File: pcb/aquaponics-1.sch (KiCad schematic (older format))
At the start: 20 parts, among them J1 5V Power Source, J2 Screw_Terminal_01x02, J3 Water Level Sensor, J4 Rain Sensor, J5 Conn_01x02_Female, M1 Growbed Pump, M2 Overflow Pump, M3 Fish Feeder, Q1 TIP120, Q2 TIP120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

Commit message: Version 2 board
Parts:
- added J6: Conn_01x04_Female, Connector_PinHeader_2.54mm:PinHeader_1x04_P2.54mm_Vertical, symbol Connector:Conn_01x04_Female
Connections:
- net +5V: now also J6.3 (Pin_3)
- net GND1: now also J6.4 (Pin_4)
- net at U1.23 (A4/D18): now also J6.1 (Pin_1)
- net at U1.24 (A5/D19): now also J6.2 (Pin_2)
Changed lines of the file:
@@
 Connection ~ 4600 1300
 $Comp
-L power:GND1 #PWR?
+L power:GND1 #PWR0101
 U 1 1 61D21553
 P 5100 2750
-F 0 "#PWR?" H 5100 2500 50  0001 C CNN
+F 0 "#PWR0101" H 5100 2500 50  0001 C CNN
 F 1 "GND1" V 5105 2622 50  0000 R CNN
 F 2 "" H 5100 2750 50  0001 C CNN
@@
 	5100 2750 5000 2750
 $Comp
-L power:GND1 #PWR?
+L power:GND1 #PWR0102
 U 1 1 61D2D750
 P 3600 2950
-F 0 "#PWR?" H 3600 2700 50  0001 C CNN
+F 0 "#PWR0102" H 3600 2700 50  0001 C CNN
 F 1 "GND1" V 3605 2822 50  0000 R CNN
 F 2 "" H 3600 2950 50  0001 C CNN
@@
 	3600 2950 3800 2950
 $Comp
-L power:GND1 #PWR?
+L power:GND1 #PWR0109
 U 1 1 61D3011A
 P 3850 1900
-F 0 "#PWR?" H 3850 1650 50  0001 C CNN
+F 0 "#PWR0109" H 3850 1650 50  0001 C CNN
 F 1 "GND1" V 3855 1772 50  0000 R CNN
 F 2 "" H 3850 1900 50  0001 C CNN
@@
 	3850 1900 4200 1900
 $Comp
-L power:GND1 #PWR?
+L power:GND1 #PWR0112
 U 1 1 61D4FBBC
 P 4400 5650
-F 0 "#PWR?" H 4400 5400 50  0001 C CNN
+F 0 "#PWR0112" H 4400 5400 50  0001 C CNN
 F 1 "GND1" H 4405 5477 50  0000 C CNN
 F 2 "" H 4400 5650 50  0001 C CNN
@@
 	4400 5650 4400 5450
 $Comp
-L power:GND1 #PWR?
+L power:GND1 #PWR0113
 U 1 1 61D6010D
 P 5800 3750
-F 0 "#PWR?" H 5800 3500 50  0001 C CNN
+F 0 "#PWR0113" H 5800 3500 50  0001 C CNN
 F 1 "GND1" V 5805 3622 50  0000 R CNN
 F 2 "" H 5800 3750 50  0001 C CNN
@@
 	5800 3750 6300 3750
 $Comp
-L power:GND1 #PWR?
+L power:GND1 #PWR0114
 U 1 1 61D69618
 P 5800 3250
-F 0 "#PWR?" H 5800 3000 50  0001 C CNN
+F 0 "#PWR0114" H 5800 3000 50  0001 C CNN
 F 1 "GND1" V 5805 3122 50  0000 R CNN
 F 2 "" H 5800 3250 50  0001 C CNN
@@
 	5800 3250 6300 3250
 $Comp
-L power:GND1 #PWR?
+L power:GND1 #PWR0115
 U 1 1 61D8D003
 P 5900 1850
-F 0 "#PWR?" H 5900 1600 50  0001 C CNN
+F 0 "#PWR0115" H 5900 1600 50  0001 C CNN
 F 1 "GND1" H 5905 1677 50  0000 C CNN
 F 2 "" H 5900 1850 50  0001 C CNN
@@
 Wire Wire Line
 	4400 4650 4950 4650
+$Comp
+L Connector:Conn_01x04_Female J6
+U 1 1 61E05BA5
+P 6450 4450
+F 0 "J6" H 6478 4426 50  0000 L CNN
+F 1 "Conn_01x04_Female" H 6478 4335 50  0000 L CNN
+F 2 "Connector_PinHeader_2.54mm:PinHeader_1x04_P2.54mm_Vertical" H 6450 4450 50  0001 C CNN
+F 3 "~" H 6450 4450 50  0001 C CNN
+	1    6450 4450
+	1    0    0    -1
+$EndComp
+Wire Wire Line
+	5000 3350 5300 3350
+Wire Wire Line
+	5300 3350 5300 4350
+Wire Wire Line
+	5300 4350 6250 4350
+Wire Wire Line
+	5000 3250 5200 3250
+Wire Wire Line
+	5200 3250 5200 4400
+Wire Wire Line
+	5200 4400 6250 4400
+Wire Wire Line
+	6250 4400 6250 4450
+$Comp
+L power:GND1 #PWR0116
+U 1 1 61E21631
+P 6000 4650
+F 0 "#PWR0116" H 6000 4400 50  0001 C CNN
+F 1 "GND1" V 6005 4522 50  0000 R CNN
+F 2 "" H 6000 4650 50  0001 C CNN
+F 3 "" H 6000 4650 50  0001 C CNN
+	1    6000 4650
+	0    1    1    0
+$EndComp
+Wire Wire Line
+	6000 4650 6250 4650
+$Comp
+L power:+5V #PWR0117
+U 1 1 61E2795D
+P 5950 4500
+F 0 "#PWR0117" H 5950 4350 50  0001 C CNN
+F 1 "+5V" V 5965 4628 50  0000 L CNN
+F 2 "" H 5950 4500 50  0001 C CNN
+F 3 "" H 5950 4500 50  0001 C CNN
+	1    5950 4500
+	0    -1   -1   0
+$EndComp
+Wire Wire Line
+	5950 4500 6100 4500
+Wire Wire Line
+	6100 4500 6100 4550
+Wire Wire Line
+	6100 4550 6250 4550
 $EndSCHEMATC

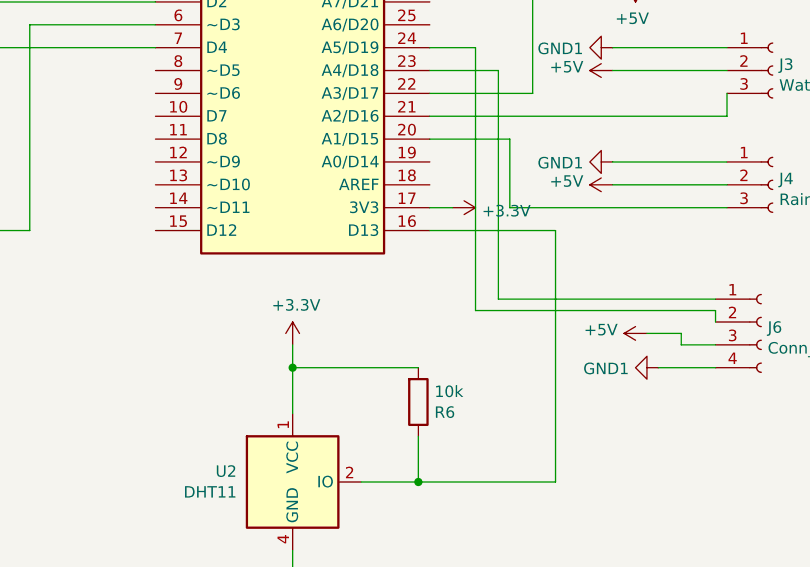
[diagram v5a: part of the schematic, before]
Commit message: Temp sensor to use 5V souce
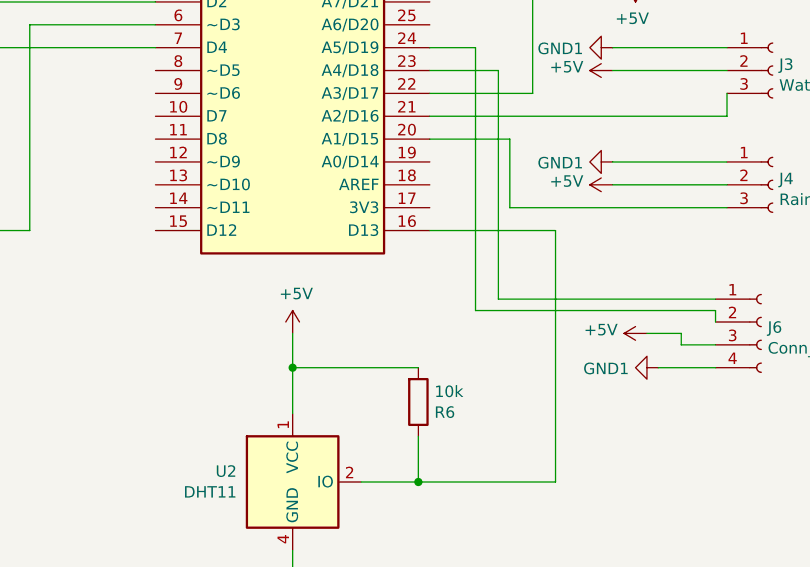
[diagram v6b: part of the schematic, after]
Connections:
- net +5V: now also R6.2, U2.1 (VCC)
- removed net +3V3: R6.2, U1.17 (3V3), U2.1 (VCC)
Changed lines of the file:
@@
 Wire Wire Line
 	5350 3650 5000 3650
-$Comp
-L power:+3.3V #PWR0103
-U 1 1 61B97206
-P 5100 3950
-F 0 "#PWR0103" H 5100 3800 50  0001 C CNN
-F 1 "+3.3V" V 5115 4078 50  0000 L CNN
-F 2 "" H 5100 3950 50  0001 C CNN
-F 3 "" H 5100 3950 50  0001 C CNN
-	1    5100 3950
-	0    1    1    0
-$EndComp
-Wire Wire Line
-	5100 3950 5000 3950
 Wire Wire Line
 	5550 5150 4950 5150
-$Comp
-L power:+3.3V #PWR0104
-U 1 1 61B9BD8B
-P 4400 4550
-F 0 "#PWR0104" H 4400 4400 50  0001 C CNN
-F 1 "+3.3V" H 4415 4723 50  0000 C CNN
-F 2 "" H 4400 4550 50  0001 C CNN
-F 3 "" H 4400 4550 50  0001 C CNN
-	1    4400 4550
-	1    0    0    -1
-$EndComp
-Wire Wire Line
-	4400 4550 4400 4650
-Connection ~ 4400 4650
-Wire Wire Line
-	4400 4650 4400 4850
 Wire Wire Line
 	4950 4950 4950 5150
@@
 Wire Wire Line
 	6100 4550 6250 4550
+$Comp
+L power:+5V #PWR0104
+U 1 1 61F8D83C
+P 4400 4500
+F 0 "#PWR0104" H 4400 4350 50  0001 C CNN
+F 1 "+5V" H 4415 4673 50  0000 C CNN
+F 2 "" H 4400 4500 50  0001 C CNN
+F 3 "" H 4400 4500 50  0001 C CNN
+	1    4400 4500
+	1    0    0    -1
+$EndComp
+Wire Wire Line
+	4400 4500 4400 4650
+Connection ~ 4400 4650
+Wire Wire Line
+	4400 4650 4400 4850
 $EndSCHEMATC
